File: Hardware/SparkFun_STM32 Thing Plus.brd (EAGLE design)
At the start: 58.4 x 22.9 mm, 130 parts, among them J3 QWIIC_RA, J6 CORTEX_DEBUG, J7 MICRO-SD, U1 MCP73831, U2 3.3V, U3 W25QXX128MBIT-6X5, U4 STM32F405RGT6, Y1 32.768kHz, Y2 12MHz

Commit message: Updated V01
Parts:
- added LOGO3: OSHW-LOGOS, SparkFun-Aesthetics:OSHW-LOGO-S
- C16, C17: value 22pF -> 15pF
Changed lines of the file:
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@@
 <layer number="45" name="Holes" color="7" fill="1" visible="yes" active="yes"/>
 <layer number="46" name="Milling" color="3" fill="1" visible="no" active="yes"/>
-<layer number="47" name="Measures" color="7" fill="1" visible="yes" active="yes"/>
+<layer number="47" name="Measures" color="7" fill="1" visible="no" active="yes"/>
 <layer number="48" name="Document" color="7" fill="1" visible="no" active="yes"/>
 <layer number="49" name="Reference" color="7" fill="1" visible="no" active="yes"/>
@@
 <attribute name="VALUE" value="12MHz" x="31.977" y="10.287" size="0.6096" layer="27" font="vector" ratio="20" rot="R270" align="top-center"/>
 </element>
-<element name="C16" library="SparkFun-Capacitors" package="0402-TIGHT" value="22pF" x="31.488" y="15.875" smashed="yes" rot="R180">
+<element name="C16" library="SparkFun-Capacitors" package="0402-TIGHT" value="15pF" x="31.488" y="15.875" smashed="yes" rot="R180">
 <attribute name="NAME" x="31.488" y="15.113" size="0.6096" layer="25" font="vector" ratio="20" rot="R180" align="bottom-center"/>
-<attribute name="PROD_ID" value="CAP-14674" x="31.488" y="15.875" size="1.778" layer="27" font="vector" ratio="15" rot="R180" display="off"/>
-<attribute name="VALUE" x="31.488" y="16.637" size="0.6096" layer="27" font="vector" ratio="20" rot="R180" align="top-center"/>
-</element>
-<element name="C17" library="SparkFun-Capacitors" package="0402-TIGHT" value="22pF" x="31.488" y="14.859" smashed="yes" rot="R180">
+<attribute name="PROD_ID" value="CAP-13063" x="31.488" y="15.875" size="1.778" layer="27" font="vector" ratio="15" rot="R180" display="off"/>
+<attribute name="VALUE" value="15pF" x="31.488" y="16.637" size="0.6096" layer="27" font="vector" ratio="20" rot="R180" align="top-center"/>
+</element>
+<element name="C17" library="SparkFun-Capacitors" package="0402-TIGHT" value="15pF" x="31.488" y="14.859" smashed="yes" rot="R180">
 <attribute name="NAME" x="31.488" y="14.097" size="0.6096" layer="25" font="vector" ratio="20" rot="R180" align="bottom-center"/>
-<attribute name="PROD_ID" value="CAP-14674" x="31.488" y="14.859" size="1.778" layer="27" font="vector" ratio="15" rot="R180" display="off"/>
-<attribute name="VALUE" x="31.488" y="15.621" size="0.6096" layer="27" font="vector" ratio="20" rot="R180" align="top-center"/>
+<attribute name="PROD_ID" value="CAP-13063" x="31.488" y="14.859" size="1.778" layer="27" font="vector" ratio="15" rot="R180" display="off"/>
+<attribute name="VALUE" value="15pF" x="31.488" y="15.621" size="0.6096" layer="27" font="vector" ratio="20" rot="R180" align="top-center"/>
 </element>
 <element name="C18" library="SparkFun-Capacitors" package="0402-TIGHT" value="22pF" x="31.488" y="13.843" smashed="yes" rot="R180">
@@
 <element name="U$64" library="output" package="STM32F405RG0" value="" x="35.941" y="11.43" smashed="yes" rot="MR90"/>
 <element name="U$65" library="SparkFun-Aesthetics" package="SFE_LOGO_FLAME_.1" value="" x="21.082" y="11.43" smashed="yes" rot="R270"/>
+<element name="LOGO3" library="SparkFun-Aesthetics" package="OSHW-LOGO-S" value="OSHW-LOGOS" x="3.81" y="11.43" smashed="yes" rot="MR90"/>
 </elements>
 <signals>
@@
 <via x="50.6476" y="13.6398" extent="1-16" drill="0.3048"/>
 <contactref element="U4" pad="18"/>
-<wire x1="38.31363125" y1="6.731" x2="38.481" y2="6.731" width="0.2032" layer="1"/>
 <wire x1="38.66" y1="5.68" x2="38.66" y2="6.552" width="0.2032" layer="1"/>
 <wire x1="38.66" y1="6.552" x2="38.481" y2="6.731" width="0.2032" layer="1"/>

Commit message: Updated version number to V10
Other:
- board text added: "v10"
- board text removed: "v01"
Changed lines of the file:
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@@
 <wire x1="44.45" y1="2.413" x2="44.45" y2="3.175" width="0.3048" layer="22"/>
 <wire x1="39.37" y1="2.413" x2="39.37" y2="3.175" width="0.3048" layer="22"/>
-<text x="0.508" y="9.906" size="1.016" layer="16" font="vector" ratio="15" rot="MR90">v01</text>
+<text x="0.508" y="9.906" size="1.016" layer="16" font="vector" ratio="15" rot="MR90">v10</text>
 <text x="26.67" y="-19.05" size="1.778" layer="51" font="vector" ratio="15">Alex Wende</text>
 <dimension x1="0" y1="0" x2="58.42" y2="0" x3="29.21" y3="-8.89" textsize="1.27" textratio="15" layer="47" unit="inch" visible="yes"/>

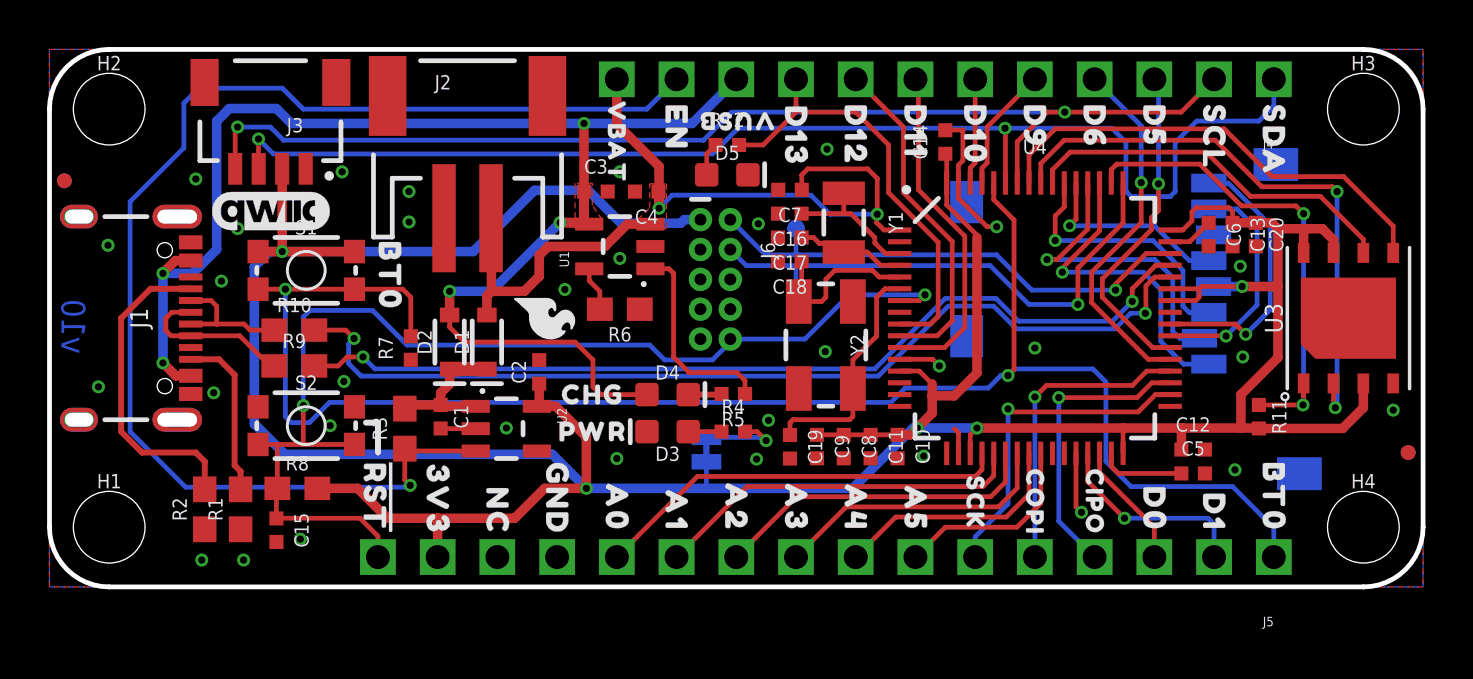
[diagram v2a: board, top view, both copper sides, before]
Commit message: V10 design review changes
Replaced V_BAT pin connection on STM32 to test point
Moved microSD connector to center card on PCB instead of footprint
Removed overlapping labels on bottom
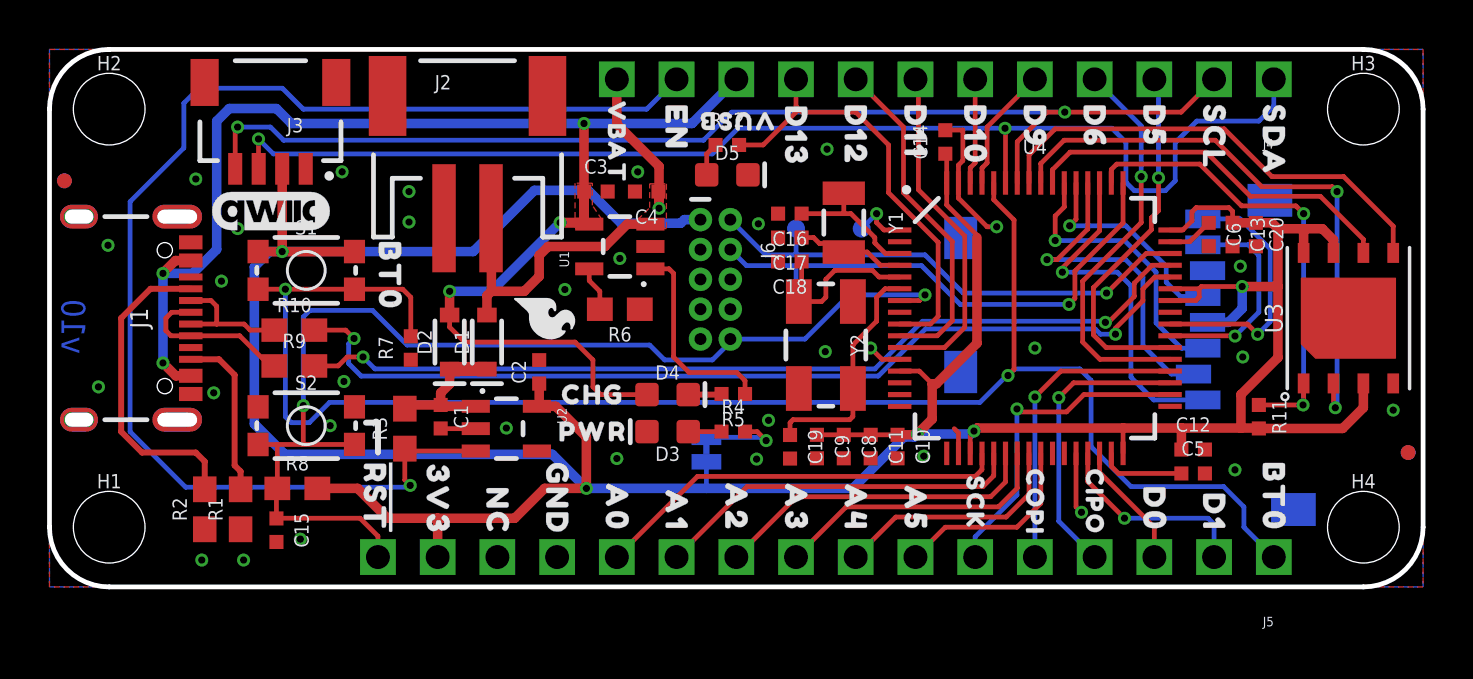
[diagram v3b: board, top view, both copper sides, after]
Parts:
- removed C7: 0.1uF, SparkFun-Capacitors:0402-TIGHT
- removed U$23: (no value), output:BT0_0
- removed U$24: (no value), output:TX_0
- removed U$25: (no value), output:RX_0
- removed U$26: (no value), output:CPIO_0
- removed U$27: (no value), output:COPI_0
- removed U$28: (no value), output:SCK_0
- added TP3: (no value), SparkFun-Connectors:PAD.03X.03
- moved J7 1.55 mm to (38.4, 16.9)
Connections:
- new net N$4: TP3.P$1, U4.1
- net GND: no longer C7.2
- net V_BATT: no longer C7.1, U4.1
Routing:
- net V_BATT: track 36.6 -> 19.6 mm, vias 2 -> 1
- net N$4: track 0.00 -> 2.39 mm, vias 0 -> 1
- net D6: track 15.5 -> 17.0 mm
- net D5: track 14.1 -> 15.6 mm
- net SDIO_D2: track 13.6 -> 15.0 mm
- net D-: track 41.4 -> 40.5 mm
- net SDIO_CLK: track 8.47 -> 9.25 mm
- net SDIO_D3: track 13.4 -> 14.2 mm
- net SDIO_CMD: track 11.3 -> 12.1 mm
- net D+: track 39.7 -> 39.0 mm
- net SDA: track 53.9 -> 53.2 mm
- net SDIO_D0: track 9.89 -> 9.19 mm
- net SDIO_D1: track 11.8 -> 11.1 mm
- net BOOT0: track 71.5 -> 70.9 mm

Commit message: Double-check changes
Schematic
- Added VDD range
- Added RTC Battery range

Board
- Updated labels
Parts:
- removed U$17: (no value), output:SDA0
- removed U$18: (no value), output:SCL0
- removed U$19: (no value), output:D5_0
- removed U$20: (no value), output:D6_0
- removed U$21: (no value), output:D9_0
- removed U$22: (no value), output:D10_0
- added U$1: (no value), buzzard_labels:D53
- added U$23: (no value), buzzard_labels:D62
- added U$24: (no value), buzzard_labels:D91
- added U$25: (no value), buzzard_labels:D100
- added U$26: (no value), buzzard_labels:SCL4
- added U$27: (no value), buzzard_labels:SDA5
- renumbered TP3 to VB
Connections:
- net N$4 renamed VB
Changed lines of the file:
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@@
 <layer number="50" name="dxf" color="7" fill="1" visible="no" active="no"/>
 <layer number="51" name="tDocu" color="6" fill="1" visible="yes" active="yes"/>
-<layer number="52" name="bDocu" color="7" fill="1" visible="yes" active="yes"/>
+<layer number="52" name="bDocu" color="7" fill="1" visible="no" active="yes"/>
 <layer number="53" name="tGND_GNDA" color="7" fill="9" visible="no" active="no"/>
 <layer number="54" name="bGND_GNDA" color="1" fill="9" visible="no" active="no"/>
@@
 </element>
 <element name="U$58" library="output" package="PWR0" value="" x="27.94" y="7.493" smashed="yes" rot="MR0"/>
-<element name="U$17" library="output" package="SDA0" value="" x="52.07" y="19.685" smashed="yes" rot="MR180"/>
-<element name="U$18" library="output" package="SCL0" value="" x="49.53" y="19.685" smashed="yes" rot="MR180"/>
-<element name="U$19" library="output" package="D5_0" value="" x="47.117" y="19.685" smashed="yes" rot="MR180"/>
-<element name="U$20" library="output" package="D6_0" value="" x="44.577" y="19.685" smashed="yes" rot="MR180"/>
-<element name="U$21" library="output" package="D9_0" value="" x="42.037" y="19.685" smashed="yes" rot="MR180"/>
-<element name="U$22" library="output" package="D10_0" value="" x="39.37" y="19.685" smashed="yes" rot="MR180"/>
 <element name="LOGO1" library="SparkFun-Aesthetics" package="QWIIC_5MM" value="QWIIC_LOGO_5MM" x="9.398" y="16.002" smashed="yes"/>
 <element name="U$59" library="output" package="SCL_0" value="" x="49.53" y="21.209" smashed="yes" rot="R270"/>
@@
 <element name="U$65" library="SparkFun-Aesthetics" package="SFE_LOGO_FLAME_.1" value="" x="21.082" y="11.43" smashed="yes" rot="R270"/>
 <element name="LOGO3" library="SparkFun-Aesthetics" package="OSHW-LOGO-S" value="OSHW-LOGOS" x="3.81" y="11.43" smashed="yes" rot="MR90"/>
-<element name="TP3" library="SparkFun-Connectors" package="PAD.03X.03" value="" x="34.544" y="15.24" smashed="yes" rot="MR0"/>
+<element name="VB" library="SparkFun-Connectors" package="PAD.03X.03" value="" x="34.544" y="15.24" smashed="yes" rot="MR0"/>
+<element name="U$1" library="buzzard_labels" package="D53" value="" x="46.99" y="17.78" smashed="yes" rot="MR90"/>
+<element name="U$23" library="buzzard_labels" package="D62" value="" x="44.45" y="17.78" smashed="yes" rot="MR90"/>
+<element name="U$24" library="buzzard_labels" package="D91" value="" x="41.91" y="17.78" smashed="yes" rot="MR90"/>
+<element name="U$25" library="buzzard_labels" package="D100" value="" x="39.37" y="17.145" smashed="yes" rot="MR90"/>
+<element name="U$26" library="buzzard_labels" package="SCL4" value="" x="49.53" y="16.891" smashed="yes" rot="MR90"/>
+<element name="U$27" library="buzzard_labels" package="SDA5" value="" x="52.07" y="16.637" smashed="yes" rot="MR90"/>
 </elements>
 <signals>
@@
 <wire x1="30.48" y1="6.223" x2="30.3403" y2="6.3627" width="0.2032" layer="16"/>
 </signal>
-<signal name="N$4">
+<signal name="VB">
 <contactref element="U4" pad="1"/>
-<contactref element="TP3" pad="P$1"/>
+<contactref element="VB" pad="P$1"/>
 <via x="35.179" y="15.875" extent="1-16" drill="0.3048"/>
 <wire x1="36.16" y1="15.18" x2="35.493" y2="15.18" width="0.2032" layer="1"/>

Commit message: BOM update
Replaced 22 ohm resistors with 0 ohm
Replaced old momentary switches to taller momentary switches
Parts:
- R10, R9: value 22 -> 0
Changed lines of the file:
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@@
 <?xml version="1.0" encoding="utf-8"?>
 <!DOCTYPE eagle SYSTEM "eagle.dtd">
-<eagle version="9.6.2">
+<eagle version="9.5.2">
 <drawing>
 <settings>
@@
 <element name="S2" library="SparkFun-Switches" package="TACTILE_SWITCH_SMD_4.6X2.8MM" value="" x="10.922" y="6.858" smashed="yes">
 <attribute name="NAME" x="10.922" y="8.382" size="0.6096" layer="25" font="vector" ratio="20" align="bottom-center"/>
-<attribute name="PROD_ID" value="SWCH-13065" x="10.922" y="6.858" size="1.778" layer="27" font="vector" ratio="15" display="off"/>
+<attribute name="PROD_ID" value="SWCH-15606" x="10.922" y="6.858" size="1.778" layer="27" font="vector" ratio="15" display="off"/>
 <attribute name="VALUE" x="10.922" y="5.334" size="0.6096" layer="27" font="vector" ratio="20" align="top-center"/>
 </element>
 <element name="S1" library="SparkFun-Switches" package="TACTILE_SWITCH_SMD_4.6X2.8MM" value="" x="10.922" y="13.462" smashed="yes">
 <attribute name="NAME" x="10.922" y="14.986" size="0.6096" layer="25" font="vector" ratio="20" align="bottom-center"/>
-<attribute name="PROD_ID" value="SWCH-13065" x="10.922" y="13.462" size="1.778" layer="27" font="vector" ratio="15" display="off"/>
+<attribute name="PROD_ID" value="SWCH-15606" x="10.922" y="13.462" size="1.778" layer="27" font="vector" ratio="15" display="off"/>
 <attribute name="VALUE" x="10.922" y="11.938" size="0.6096" layer="27" font="vector" ratio="20" align="top-center"/>
 </element>
@@
 <attribute name="VALUE" x="8.89" y="2.413" size="0.6096" layer="27" font="vector" ratio="20" rot="R270" align="top-center"/>
 </element>
-<element name="R9" library="SparkFun-Resistors" package="0603" value="22" x="10.414" y="9.398" smashed="yes">
+<element name="R9" library="SparkFun-Resistors" package="0603" value="0" x="10.414" y="9.398" smashed="yes">
 <attribute name="NAME" x="10.414" y="10.16" size="0.6096" layer="25" font="vector" ratio="20" align="bottom-center"/>
-<attribute name="PROD_ID" value="RES-08698" x="10.414" y="9.398" size="1.778" layer="27" font="vector" ratio="15" display="off"/>
-<attribute name="VALUE" x="10.414" y="8.636" size="0.6096" layer="27" font="vector" ratio="20" align="top-center"/>
-</element>
-<element name="R10" library="SparkFun-Resistors" package="0603" value="22" x="10.414" y="10.922" smashed="yes">
+<attribute name="PROD_ID" value="RES-08609" x="10.414" y="9.398" size="1.778" layer="27" font="vector" ratio="15" display="off"/>
+<attribute name="VALUE" value="0" x="10.414" y="8.636" size="0.6096" layer="27" font="vector" ratio="20" align="top-center"/>
+</element>
+<element name="R10" library="SparkFun-Resistors" package="0603" value="0" x="10.414" y="10.922" smashed="yes">
 <attribute name="NAME" x="10.414" y="11.684" size="0.6096" layer="25" font="vector" ratio="20" align="bottom-center"/>
-<attribute name="PROD_ID" value="RES-08698" x="10.414" y="10.922" size="1.778" layer="27" font="vector" ratio="15" display="off"/>
-<attribute name="VALUE" x="10.414" y="10.16" size="0.6096" layer="27" font="vector" ratio="20" align="top-center"/>
+<attribute name="PROD_ID" value="RES-08609" x="10.414" y="10.922" size="1.778" layer="27" font="vector" ratio="15" display="off"/>
+<attribute name="VALUE" value="0" x="10.414" y="10.16" size="0.6096" layer="27" font="vector" ratio="20" align="top-center"/>
 </element>
 <element name="C20" library="SparkFun-Capacitors" package="0402-TIGHT" value="0.1uF" x="51.308" y="14.986" smashed="yes" rot="R270">

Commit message: Updated USB Load Resistors
Switch 0 ohm resistors back to 22 ohm
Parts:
- R10, R9: value 0 -> 22
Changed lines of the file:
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@@
 <?xml version="1.0" encoding="utf-8"?>
 <!DOCTYPE eagle SYSTEM "eagle.dtd">
-<eagle version="9.5.2">
+<eagle version="9.6.2">
 <drawing>
 <settings>
@@
 <attribute name="VALUE" x="8.89" y="2.413" size="0.6096" layer="27" font="vector" ratio="20" rot="R270" align="top-center"/>
 </element>
-<element name="R9" library="SparkFun-Resistors" package="0603" value="0" x="10.414" y="9.398" smashed="yes">
+<element name="R9" library="SparkFun-Resistors" package="0603" value="22" x="10.414" y="9.398" smashed="yes">
 <attribute name="NAME" x="10.414" y="10.16" size="0.6096" layer="25" font="vector" ratio="20" align="bottom-center"/>
-<attribute name="PROD_ID" value="RES-08609" x="10.414" y="9.398" size="1.778" layer="27" font="vector" ratio="15" display="off"/>
-<attribute name="VALUE" value="0" x="10.414" y="8.636" size="0.6096" layer="27" font="vector" ratio="20" align="top-center"/>
-</element>
-<element name="R10" library="SparkFun-Resistors" package="0603" value="0" x="10.414" y="10.922" smashed="yes">
+<attribute name="PROD_ID" value="RES-08698" x="10.414" y="9.398" size="1.778" layer="27" font="vector" ratio="15" display="off"/>
+<attribute name="VALUE" value="22" x="10.414" y="8.636" size="0.6096" layer="27" font="vector" ratio="20" align="top-center"/>
+</element>
+<element name="R10" library="SparkFun-Resistors" package="0603" value="22" x="10.414" y="10.922" smashed="yes">
 <attribute name="NAME" x="10.414" y="11.684" size="0.6096" layer="25" font="vector" ratio="20" align="bottom-center"/>
-<attribute name="PROD_ID" value="RES-08609" x="10.414" y="10.922" size="1.778" layer="27" font="vector" ratio="15" display="off"/>
-<attribute name="VALUE" value="0" x="10.414" y="10.16" size="0.6096" layer="27" font="vector" ratio="20" align="top-center"/>
+<attribute name="PROD_ID" value="RES-08698" x="10.414" y="10.922" size="1.778" layer="27" font="vector" ratio="15" display="off"/>
+<attribute name="VALUE" value="22" x="10.414" y="10.16" size="0.6096" layer="27" font="vector" ratio="20" align="top-center"/>
 </element>
 <element name="C20" library="SparkFun-Capacitors" package="0402-TIGHT" value="0.1uF" x="51.308" y="14.986" smashed="yes" rot="R270">
